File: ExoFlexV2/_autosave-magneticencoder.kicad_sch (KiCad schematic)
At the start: 24 parts

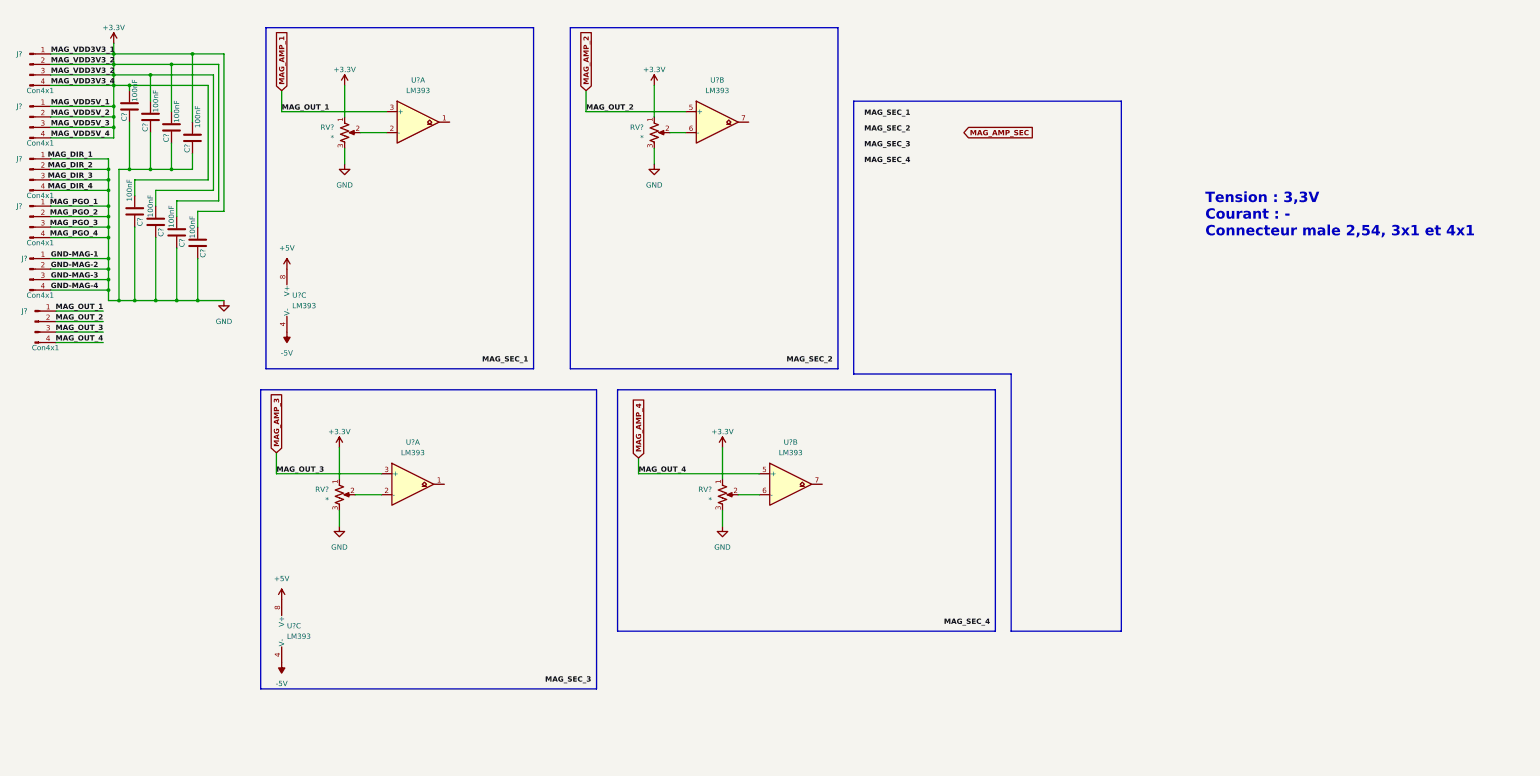
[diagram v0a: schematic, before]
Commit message: Many changes
Debouncing, power protection, potentiometer limits, etc.
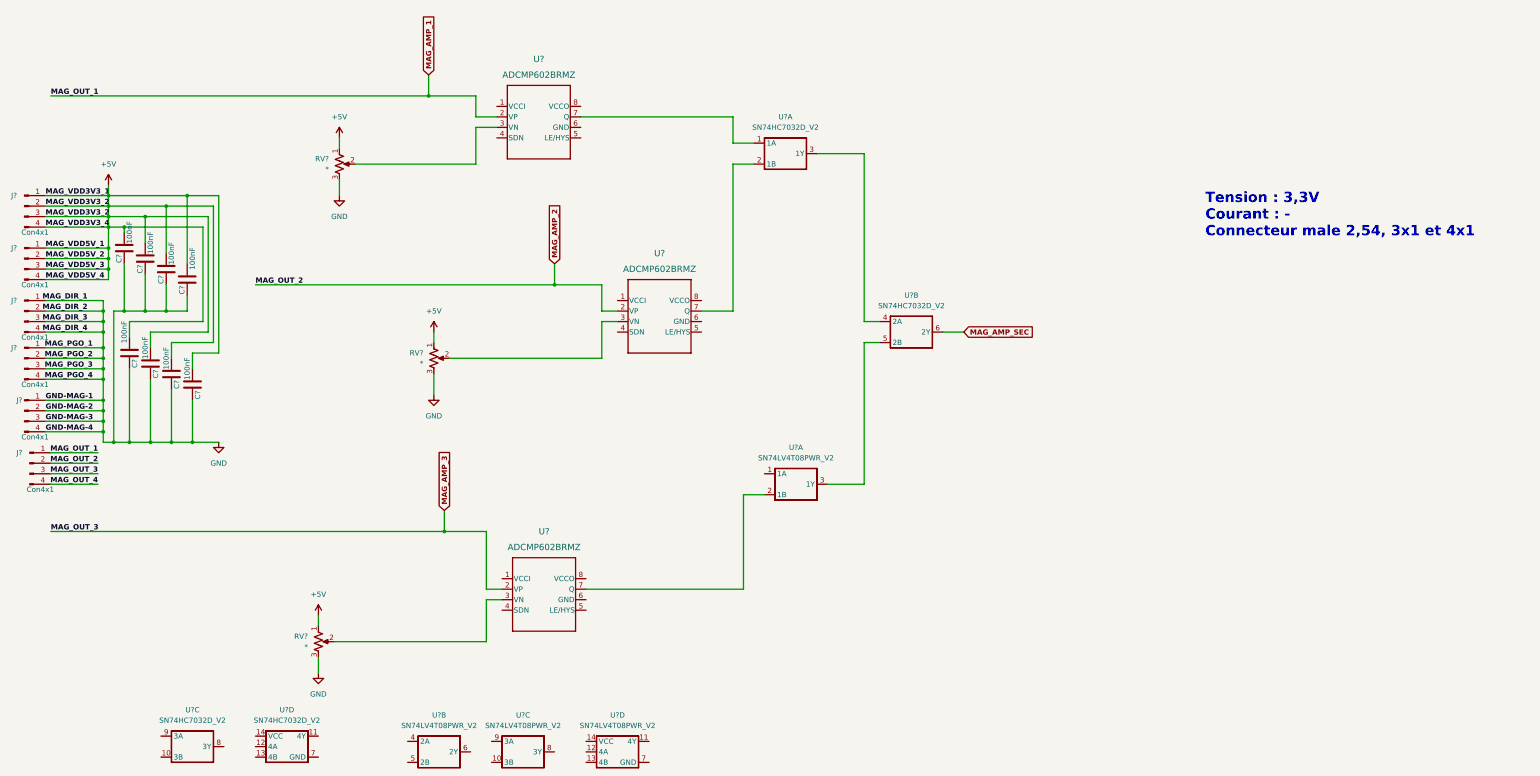
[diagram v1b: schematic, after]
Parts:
- removed RV?: *, symbol Device:R_Potentiometer_US
- removed U? (x6): LM393, symbol Comparator:LM393
- added U? (x4): SN74LV4T08PWR_V2, symbol SymLib:SN74LV4T08PWR_V2
- added U? (x4): SN74HC7032D_V2, symbol SymLib:SN74HC7032D_V2
- added U? (x3): ADCMP602BRMZ, RM_8_ADI, symbol SymLib:ADCMP602BRMZ
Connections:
- net +3.3V is gone; now on net +5V: C?.1, C?.1, C?.2, C?.2, C?.2, C?.2, C?.2, C?.2, J?.1 (Pin_1), J?.1 (Pin_1), J?.2 (Pin_2), J?.2 (Pin_2), J?.3 (Pin_3), J?.3 (Pin_3), J?.4 (Pin_4), J?.4 (Pin_4), RV?.1, RV?.1, RV?.1
- net MAG_AMP_1: now also U?.2 (VP)
- net MAG_AMP_2: now also U?.2 (VP)
- net MAG_AMP_3: now also U?.2 (VP)
- net MAG_AMP_SEC: now also U?.6 (2Y)
- net at RV?.2: now also U?.3 (VN) (x3)
- net MAG_AMP_4 renamed MAG_OUT_4
- new net: U?.1 (1A), U?.7 (Q)
- new net: U?.2 (1B), U?.7 (Q) (x2)
- new net: U?.3 (1Y), U?.4 (2A)
- new net: U?.3 (1Y), U?.5 (2B)
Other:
- moved on the sheet: C?, J?, RV?
